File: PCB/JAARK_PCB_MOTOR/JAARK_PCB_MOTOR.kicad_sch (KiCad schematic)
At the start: 12 parts, among them IC1 TPS564242DRLR

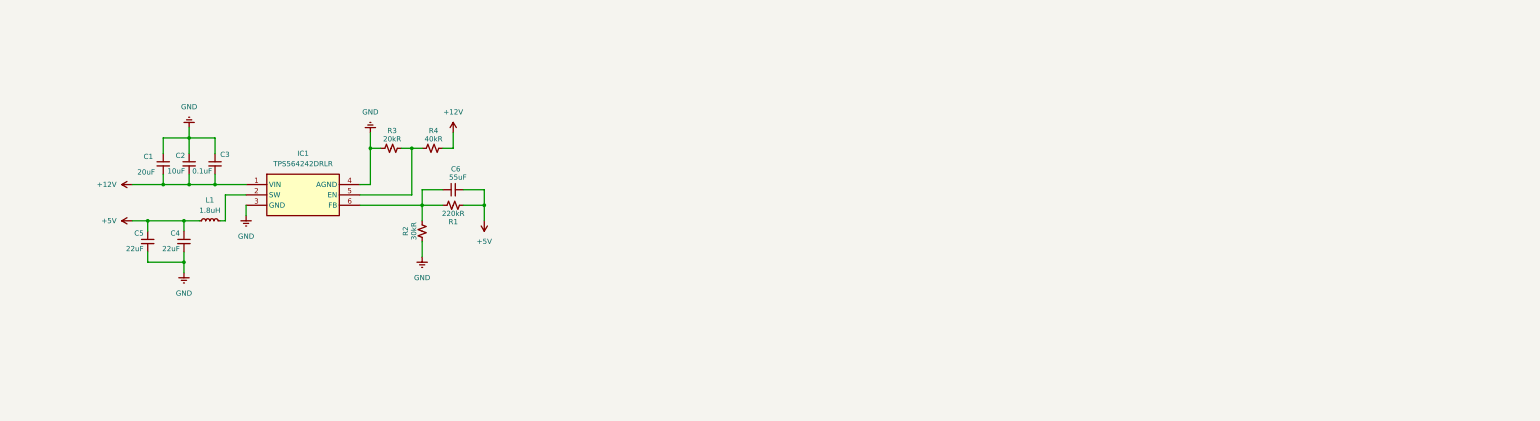
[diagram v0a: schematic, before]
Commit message: Work on Motor Driver H-Bridge. May need to consider switching to MOSFET, as BJT's are not suitable for high amp loads. Could fry board or resistors with the current H-Bridge setup.
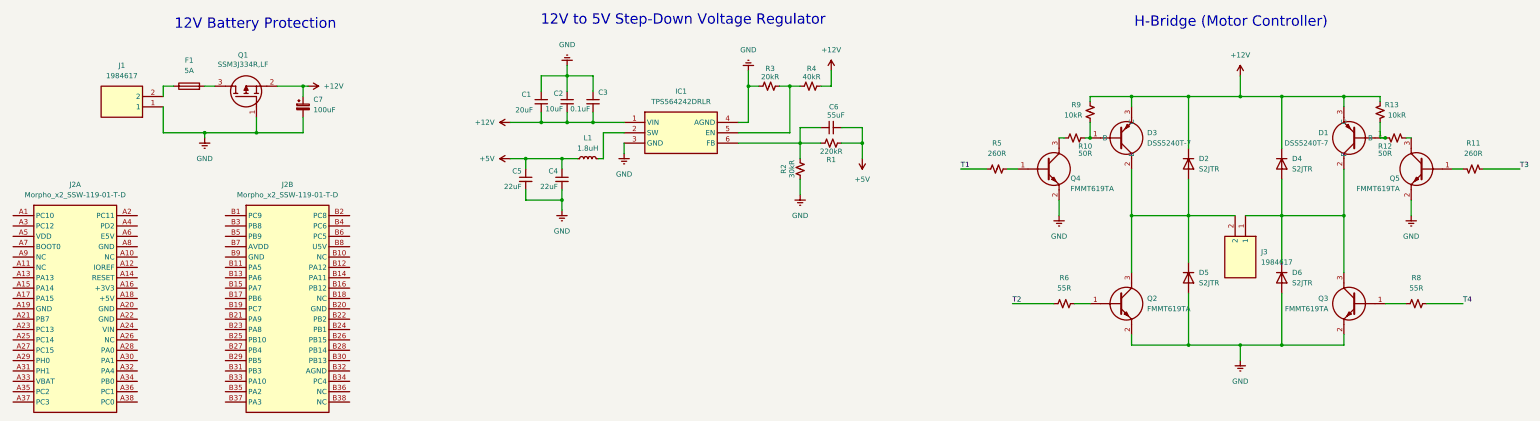
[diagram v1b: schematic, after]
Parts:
- added C7: 100uF, symbol Device:C_Polarized_Small
- added D1, D3: DSS5240T-7, SOT96P240X110-3N, symbol SSys_Parts:DSS5240T-7
- added D2, D4, D5, D6: S2JTR, Diode_SMD:D_SMB, symbol Diode:S2JTR
- added F1: 5A, symbol Device:Fuse
- added J1, J3: 1984617, 1984617, symbol SSys_Parts:1984617
- added J2: Morpho_x2_SSW-119-01-T-D, footprint_library:STM_Nucleo_Morpho_x2_Footprint, symbol sym_library:Morpho_x2_SSW-119-01-T-D
- added Q1: SSM3J334R,LF, 2SC2712GRLF, symbol SSys_Parts:SSM3J334R,LF
- added Q2, Q3, Q4, Q5: FMMT619TA, SOT95P237X112-3N, symbol SSys_Parts:FMMT619TA
- added R10, R12: 50R, symbol Device:R_Small_US
- added R11, R5: 260R, symbol Device:R_Small_US
- added R13, R9: 10kR, symbol Device:R_Small_US
- added R6, R8: 55R, symbol Device:R_Small_US
- IC1: footprint SOTFL50P160X60-6N -> SSys_Footprints:SOTFL50P160X60-6N
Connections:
- net +12V: now also C7.1, D1.3 (C), D2.1 (K), D3.3 (C), D4.1 (K), Q1.2 (S), R13.1, R9.1
- net GND: now also C7.2, D5.2 (A), D6.2 (A), J1.1, Q1.1 (G), Q2.2 (E), Q3.2 (E), Q4.2 (E), Q5.2 (E)
- new net: F1.1, J1.2
- new net: D1.1 (B), R12.2, R13.2
- new net: Q5.1 (B), R11.2
- new net: Q5.3 (C), R12.1
- new net: D1.2 (E), D4.2 (A), D6.1 (K), J3.1, Q3.3 (C)
- new net: D2.2 (A), D3.2 (E), D5.1 (K), J3.2, Q2.3 (C)
- new net: Q3.1 (B), R8.1
- new net: Q2.1 (B), R6.2
- new net: F1.2, Q1.3 (D)
- new net: D3.1 (B), R10.2, R9.2
- new net: Q4.1 (B), R5.2
- new net: Q4.3 (C), R10.1
- new net T1: R5.1
- new net T2: R6.1
- new net T3: R11.1
- new net T4: R8.2
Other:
- note added: "12V Battery Protection"
- note added: "12V to 5V Step-Down Voltage Regulator"
- note added: "H-Bridge (Motor Controller)"
- moved on the sheet: C1, C2, C3, C4, C5, C6, IC1, L1, R1, R2, R3, R4

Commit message: Finished H-Bridge
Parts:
- removed D1, D3: DSS5240T-7, SOT96P240X110-3N, symbol SSys_Parts:DSS5240T-7
- removed D2, D4, D5, D6: S2JTR, Diode_SMD:D_SMB, symbol Diode:S2JTR
- removed J3: 1984617, 1984617, symbol SSys_Parts:1984617
- removed Q2: FMMT619TA, SOT95P237X112-3N, symbol SSys_Parts:FMMT619TA
- removed R10, R12: 50R, symbol Device:R_Small_US
- removed R11, R5: 260R, symbol Device:R_Small_US
- removed R13, R9: 10kR, symbol Device:R_Small_US
- removed R6, R8: 55R, symbol Device:R_Small_US
- added D10, D11, D8, D9: S2JTR, Diode_SMD:D_SMB, symbol Diode:S2JTR
- added IC2, IC3: PJA3404_R1_00001, SOT95P240X110-3N, symbol SSys_Parts:PJA3404_R1_00001
- added J4: ${SIM.PARAMS}, 1984617, symbol SSys_Parts:1984617
- added Q2, Q6: SSM3J334RLF, 2SC2712GRLF, symbol SSys_Parts:SSM3J334R,LF
- added Q7: FMMT619TA, SOT95P237X112-3N, symbol SSys_Parts:FMMT619TA
- added R14, R16, R21, R22: 260R, symbol Device:R_Small_US
- added R15, R17, R18, R7: 5kR, symbol Device:R_Small_US
- added R19, R20: 10kR, symbol Device:R_Small_US
- added V1: 12, symbol Simulation_SPICE:VDC
- added V2: 3.3, symbol Simulation_SPICE:VDC
- added V3: 0, symbol Simulation_SPICE:VDC
- J1: value 1984617 -> ${SIM.PARAMS}
- Q1: value SSM3J334R,LF -> SSM3J334RLF; Spice_Node_Sequence (none) -> 3 1 2 2
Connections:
- net +12V: now also D10.1 (K), D8.1 (K), Q2.2 (S), Q6.2 (S), R15.1, R18.2, R19.1, R20.1
- net GND: now also D11.2 (A), D9.2 (A), IC2.2 (S), IC3.2 (S), Q7.2 (E), V1.2, V2.2, V3.2
- net T1: now also R14.2, R21.2, V3.1
- net T2: now also R16.2, R22.1, V2.1
- net at F1.1, J1.2: now also V1.1
- net at Q5.1 (B): now also R16.1
- net at Q5.3 (C): now also R17.2
- net at Q3.3 (C): now also IC3.1 (G), R20.2
- net at Q3.1 (B): now also R22.2
- net at Q4.1 (B): now also R14.1
- net at Q4.3 (C): now also R7.2
- new net: Q6.1 (G), R17.1, R18.1
- new net: D8.2 (A), D9.1 (K), IC2.3 (D), J4.2, Q2.3 (D)
- new net: IC2.1 (G), Q7.3 (C), R19.2
- new net: Q7.1 (B), R21.1
- new net: D10.2 (A), D11.1 (K), IC3.3 (D), J4.1, Q6.3 (D)
- new net: Q2.1 (G), R15.2, R7.1
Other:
- moved on the sheet: J1

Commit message: Organizing libraries in the local folder.
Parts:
- IC1: footprint SSys_Footprints:SOTFL50P160X60-6N -> JAARK_lib:SOTFL50P160X60-6N
- IC2, IC3: footprint SOT95P240X110-3N -> SSys_Footprints:SOT95P240X110-3N
- J1, J4: footprint 1984617 -> SSys_Footprints:1984617
- Q1, Q2, Q6: footprint 2SC2712GRLF -> SSys_Footprints:2SC2712GRLF
- Q3, Q4, Q5, Q7: footprint SOT95P237X112-3N -> SSys_Footprints:SOT95P237X112-3N
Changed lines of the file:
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@@
 			)
 		)
-		(property "Footprint" "1984617"
+		(property "Footprint" "SSys_Footprints:1984617"
 			(at 34.29 -51.74 0)
 			(effects
@@
 			)
 		)
-		(property "Footprint" "SOT95P240X110-3N"
+		(property "Footprint" "SSys_Footprints:SOT95P240X110-3N"
 			(at 297.18 183.82 0)
 			(effects
@@
 			)
 		)
-		(property "Footprint" "SOT95P240X110-3N"
+		(property "Footprint" "SSys_Footprints:SOT95P240X110-3N"
 			(at 339.09 183.82 0)
 			(effects
@@
 			)
 		)
-		(property "Footprint" "SOT95P237X112-3N"
+		(property "Footprint" "SSys_Footprints:SOT95P237X112-3N"
 			(at 280.67 216.84 0)
 			(effects
@@
 			)
 		)
-		(property "Footprint" "1984617"
+		(property "Footprint" "SSys_Footprints:1984617"
 			(at 225.12 83.82 0)
 			(effects
@@
 			)
 		)
-		(property "Footprint" "2SC2712GRLF"
+		(property "Footprint" "SSys_Footprints:2SC2712GRLF"
 			(at 186.36 34.29 0)
 			(effects
@@
 			)
 		)
-		(property "Footprint" "SOT95P237X112-3N"
+		(property "Footprint" "SSys_Footprints:SOT95P237X112-3N"
 			(at 355.6 216.84 0)
 			(effects
@@
 			)
 		)
-		(property "Footprint" "SOT95P237X112-3N"
+		(property "Footprint" "SSys_Footprints:SOT95P237X112-3N"
 			(at 280.67 160.96 0)
 			(effects
@@
 			)
 		)
-		(property "Footprint" "2SC2712GRLF"
+		(property "Footprint" "SSys_Footprints:2SC2712GRLF"
 			(at 340.36 -53.01 0)
 			(effects
@@
 			)
 		)
-		(property "Footprint" "SOT95P237X112-3N"
+		(property "Footprint" "SSys_Footprints:SOT95P237X112-3N"
 			(at 355.6 160.96 0)
 			(effects
@@
 			)
 		)
-		(property "Footprint" "SSys_Footprints:SOTFL50P160X60-6N"
+		(property "Footprint" "JAARK_lib:SOTFL50P160X60-6N"
 			(at 201.93 141.91 0)
 			(effects
@@
 			)
 		)
-		(property "Footprint" "2SC2712GRLF"
+		(property "Footprint" "SSys_Footprints:2SC2712GRLF"
 			(at 295.91 -53.01 0)
 			(effects

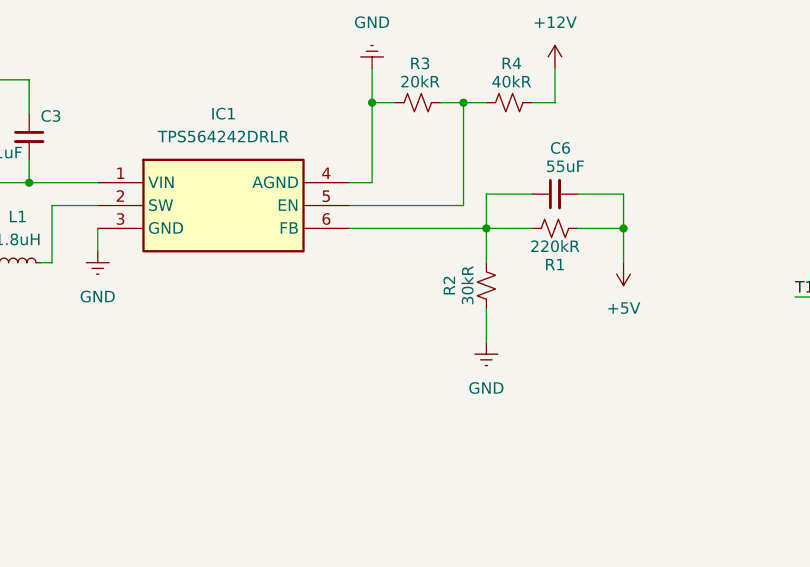
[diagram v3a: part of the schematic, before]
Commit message: Starting zephyr testing
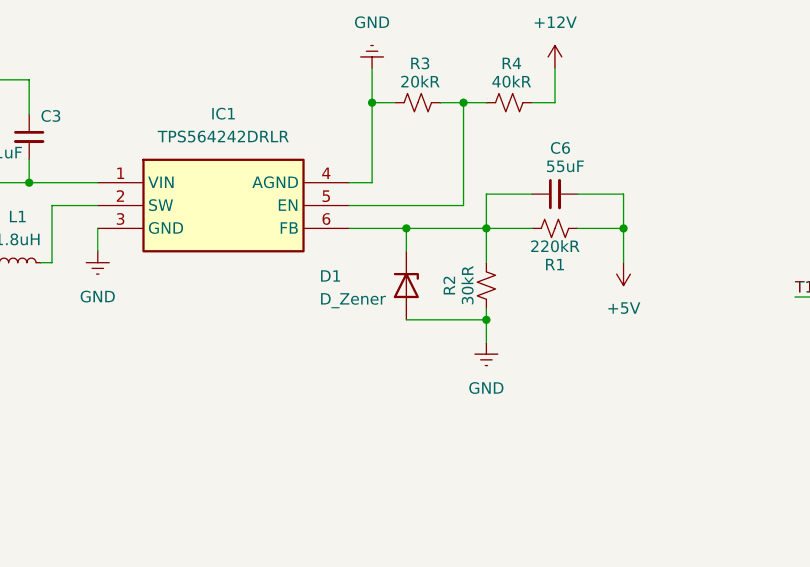
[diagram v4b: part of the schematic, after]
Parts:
- added D1: D_Zener, symbol Device:D_Zener
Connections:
- net GND: now also D1.2 (A)
- net at C6.1, IC1.6 (FB), R1.2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: now also D1.1 (K)
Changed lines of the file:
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@@
 	)
 	(junction
+		(at 220.98 62.23)
+		(diameter 0)
+		(color 0 0 0 0)
+	)
+	(junction
 		(at 236.22 52.07)
 		(diameter 0)
@@
 	)
 	(junction
+		(at 212.09 52.07)
+		(diameter 0)
+		(color 0 0 0 0)
+	)
+	(junction
 		(at 162.56 66.04)
 		(diameter 0)
@@
 	(wire
 		(pts
-			(xy 205.74 52.07) (xy 220.98 52.07)
+			(xy 205.74 52.07) (xy 212.09 52.07)
 		)
 		(stroke
@@
 	(wire
 		(pts
+			(xy 212.09 62.23) (xy 220.98 62.23)
+		)
+		(stroke
+			(width 0)
+			(type default)
+		)
+	)
+	(wire
+		(pts
+			(xy 212.09 52.07) (xy 220.98 52.07)
+		)
+		(stroke
+			(width 0)
+			(type default)
+		)
+	)
+	(wire
+		(pts
 			(xy 328.93 67.31) (xy 328.93 90.17)
 		)
@@
 	(wire
 		(pts
-			(xy 220.98 60.96) (xy 220.98 64.77)
+			(xy 220.98 60.96) (xy 220.98 62.23)
 		)
 		(stroke
@@
 	(wire
 		(pts
+			(xy 212.09 52.07) (xy 212.09 54.61)
+		)
+		(stroke
+			(width 0)
+			(type default)
+		)
+	)
+	(wire
+		(pts
 			(xy 292.1 38.1) (xy 306.07 38.1)
 		)
@@
 	(wire
 		(pts
+			(xy 220.98 62.23) (xy 220.98 64.77)
+		)
+		(stroke
+			(width 0)
+			(type default)
+		)
+	)
+	(wire
+		(pts
 			(xy 344.17 67.31) (xy 344.17 55.88)
 		)
@@
 					(unit 1)
 				)
+			)
+		)
+	)
+	(symbol
+		(lib_id "Device:D_Zener")
+		(at 212.09 58.42 270)
+		(unit 1)
+		(exclude_from_sim no)
+		(in_bom yes)
+		(on_board yes)
+		(dnp no)
+		(property "Reference" "D1"
+			(at 202.438 57.404 90)
+			(effects
+				(font
+					(size 1.27 1.27)
+				)
+				(justify left)
+			)
+		)
+		(property "Value" "D_Zener"
+			(at 202.438 59.944 90)
+			(effects
+				(font
+					(size 1.27 1.27)
+				)
+				(justify left)
+			)
+		)
+		(property "Footprint" ""
+			(at 212.09 58.42 0)
+			(effects
+				(font
+					(size 1.27 1.27)
+				)
+				(hide yes)
+			)
+		)
+		(property "Datasheet" "~"
+			(at 212.09 58.42 0)
+			(effects
+				(font
+					(size 1.27 1.27)
+				)
+				(hide yes)
+			)
+		)
+		(property "Description" "Zener diode"
+			(at 212.09 58.42 0)
+			(effects
+				(font
+					(size 1.27 1.27)
+				)
+				(hide yes)
+			)
+		)
+		(pin "1"
+		)
+		(pin "2"
+		)
+		(instances
+			(project ""
+				(path "/855a2ad7-0ca6-4188-a452-4c1fc0d76ca5"
+					(reference "D1")
+					(unit 1)
+				)

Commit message: Motor driver recreation, appended footprints to lots of R,L,C elements
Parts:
- removed IC3: PJA3404_R1_00001, SSys_Footprints:SOT95P240X110-3N, symbol SSys_Parts:PJA3404_R1_00001
- added C8: 22uF, JAARK_lib:CAPC2012X95N, symbol JAARK_lib:CL21B104KBCNNNC
- added IC3, IC5, IC6, IC7, IC8: PJA3404_R1_00001, SOT95P240X110-3N, symbol JAARK_lib:SSM3J334R,LF
- added IC4: HIP4080AIBZT, SOIC127P1032X265-20N, symbol JAARK_lib:HIP4080AIBZT
- added J3: ~, SSys_Footprints:1984617, symbol SSys_Parts:1984617
- C1: value 20uF -> 22uF; footprint (none) -> JAARK_lib:CAPC2012X95N; symbol Device:C_Small -> JAARK_lib:CL21B104KBCNNNC; Arrow Part Number (none) -> CL21B104KBCNNNC; Arrow Price/Stock (none) -> https://www.arrow.com/en/products/cl21b104kbcnnnc/samsung-e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; Height (none) -> 0.95; MPN (none) -> CL21A226MAYNNNE; Manufacturer_Name (none) -> SAMSUNG; Manufacturer_Part_Number (none) -> CL21B104KBCNNNC; Mouser Part Number (none) -> 187-CL21B104KBCNNNC; Mouser Price/Stock (none) -> https://www.mouser.co.uk/ProductDetail/Samsung-Electro-Mech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
- C2: footprint (none) -> JAARK_lib:CAPC2012X145N; Arrow Part Number (none) -> CL21A106KAYNNNG; Arrow Price/Stock (none) -> https://www.arrow.com/en/products/cl21a106kaynnng/samsung-e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; Height (none) -> 1.45; Manufacturer_Name (none) -> SAMSUNG; Manufacturer_Part_Number (none) -> CL21A106KAYNNNG; Mouser Part Number (none) -> 187-CL21A106KAYNNNG; Mouser Price/Stock (none) -> https://www.mouser.co.uk/ProductDetail/Samsung-Electro-Mech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
- C3: footprint (none) -> C0805; Arrow Part Number (none) -> C0805C104K5RACTU; Arrow Price/Stock (none) -> https://www.arrow.com/en/products/c0805c104k5ractu/kemet-co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; Height (none) -> 1.1; Manufacturer_Name (none) -> KEMET; Manufacturer_Part_Number (none) -> C0805C104K5RACTU; Mouser Part Number (none) -> 80-C0805C104K5R; Mouser Price/Stock (none) -> https://www.mouser.co.uk/ProductDetail/KEMET/C0805C104K5RAC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
- C4, C5: footprint (none) -> JAARK_lib:CAPC2012X95N; symbol Device:C_Small -> JAARK_lib:CL21B104KBCNNNC; Arrow Part Number (none) -> CL21B104KBCNNNC; Arrow Price/Stock (none) -> https://www.arrow.com/en/products/cl21b104kbcnnnc/samsung-e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; Height (none) -> 0.95; Manufacturer_Name (none) -> SAMSUNG; Manufacturer_Part_Number (none) -> CL21B104KBCNNNC; Mouser Part Number (none) -> 187-CL21B104KBCNNNC; Mouser Price/Stock (none) -> https://www.mouser.co.uk/ProductDetail/Samsung-Electro-Mech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
- C6: value 55uF -> 33uF; footprint (none) -> JAARK_lib:CAPC3216X180N; Arrow Part Number (none) -> C3216X5R1E336M160AC; Arrow Price/Stock (none) -> https://www.arrow.com/en/products/c3216x5r1e336m160ac/tdk; Height (none) -> 1.8; Manufacturer_Name (none) -> TDK; Manufacturer_Part_Number (none) -> C3216X5R1E336M160AC; Mouser Part Number (none) -> 810-C3216X5R1E336M; Mouser Price/Stock (none) -> https://www.mouser.co.uk/ProductDetail/TDK/C3216X5R1E336M16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
- IC2: footprint SSys_Footprints:SOT95P240X110-3N -> SOT95P240X110-3N; symbol SSys_Parts:PJA3404_R1_00001 -> JAARK_lib:SSM3J334R,LF
- J1: value ${SIM.PARAMS} -> dc=12
- J4: value ${SIM.PARAMS} -> ~
- L1: footprint (none) -> INDPM4141X200N; Height (none) -> 2; Manufacturer_Name (none) -> Wurth Elektronik; Manufacturer_Part_Number (none) -> 74438356018; Mouser Part Number (none) -> 710-74438356018; Mouser Price/Stock (none) -> https://www.mouser.co.uk/ProductDetail/Wurth-Elektronik/744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
- Q1, Q2, Q6: footprint SSys_Footprints:2SC2712GRLF -> 2SC2712GRLF; symbol SSys_Parts:SSM3J334R,LF -> JAARK_lib:SSM3J334R,LF
- Q3, Q4, Q5, Q7: footprint SSys_Footprints:SOT95P237X112-3N -> SOT95P237X112-3N; symbol SSys_Parts:FMMT619TA -> JAARK_lib:FMMT619TA
- R1: footprint (none) -> RESC2012X65N; Arrow Part Number (none) -> CRG0805F220K; Arrow Price/Stock (none) -> https://www.arrow.com/en/products/crg0805f220k/te-connectiv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; Height (none) -> 0.65; Manufacturer_Name (none) -> TE Connectivity; Manufacturer_Part_Number (none) -> CRG0805F220K; Mouser Part Number (none) -> 279-CRG0805F220K; Mouser Price/Stock (none) -> https://www.mouser.co.uk/ProductDetail/TE-Connectivity-Hols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
- R14, R16, R21, R22: footprint (none) -> RESC2012X60N; Height (none) -> 0.6; Manufacturer_Name (none) -> KEMET; Manufacturer_Part_Number (none) -> RC0805FR-07261RL
- R15, R17, R18, R7: footprint (none) -> RESC2012X50N; Arrow Part Number (none) -> CRCW08055K00FKTA; Arrow Price/Stock (none) -> https://www.arrow.com/en/products/crcw08055k00fkta/vishay?r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; Height (none) -> 0.5; Manufacturer_Name (none) -> Vishay; Manufacturer_Part_Number (none) -> CRCW08055K00FKTA; Mouser Part Number (none) -> 71-CRCW0805-5K; Mouser Price/Stock (none) -> https://www.mouser.co.uk/ProductDetail/Vishay-Dale/CRCW0805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
- R19, R20: footprint (none) -> RESC2012X60N; Arrow Part Number (none) -> RC0805JR-0710KL; Arrow Price/Stock (none) -> https://www.arrow.com/en/products/rc0805jr-0710kl/yageo; Height (none) -> 0.6; Manufacturer_Name (none) -> KEMET; Manufacturer_Part_Number (none) -> RC0805JR-0710KL; Mouser Part Number (none) -> 603-RC0805JR-0710KL; Mouser Price/Stock (none) -> https://www.mouser.co.uk/ProductDetail/YAGEO/RC0805JR-0710K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
- R2: footprint (none) -> RESC2012X60N; Arrow Part Number (none) -> RC0805FR-0730K1L; Arrow Price/Stock (none) -> https://www.arrow.com/en/products/rc0805fr-0730k1l/yageo?re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; Height (none) -> 0.6; Manufacturer_Name (none) -> KEMET; Manufacturer_Part_Number (none) -> RC0805FR-0730K1L; Mouser Part Number (none) -> 603-RC0805FR-0730K1L; Mouser Price/Stock (none) -> https://www.mouser.com/Search/Refine.aspx?Keyword=603-RC080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
- R3: footprint (none) -> RESC2012X50N; Height (none) -> 0.5; Manufacturer_Name (none) -> Susumu; Manufacturer_Part_Number (none) -> RG2012P-203-B-T5; Mouser Part Number (none) -> 754-RG2012P-203-B-T5; Mouser Price/Stock (none) -> https://www.mouser.co.uk/ProductDetail/Susumu/RG2012P-203-B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
- R4: footprint (none) -> JAARK_lib:RESC2012X60N; Arrow Part Number (none) -> RC0805FR-0740K2L; Arrow Price/Stock (none) -> https://www.arrow.com/en/products/rc0805fr-0740k2l/yageo; Height (none) -> 0.6; Manufacturer_Name (none) -> KEMET; Manufacturer_Part_Number (none) -> RC0805FR-0740K2L; Mouser Part Number (none) -> 603-RC0805FR-0740K2L; Mouser Price/Stock (none) -> https://www.mouser.co.uk/ProductDetail/Yageo/RC0805FR-0740K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
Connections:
- net +12V: now also C1.1; no longer C1.2
- net +5V: now also C4.2, C5.2, C8.1; no longer C4.1, C5.1
- net GND: now also C1.2, C4.1, C5.1, IC3.2 (S); no longer C1.1, C4.2, C5.2
- net at Q3.3 (C), R20.2: now also IC3.1 (G)
- net at D10.2 (A), D11.1 (K), J4.1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: now also IC3.3 (D)
- net at C6.1, D1.1 (K), IC1.6 (FB)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: now also C8.2
- new net: IC4.20 (BHO), IC5.1 (G)
- new net: IC4.19 (BHS), IC5.2 (S), IC6.3 (D), J3.2
- new net: IC5.3 (D), IC7.3 (D)
- new net: IC4.18 (BLO), IC6.1 (G)
- new net: IC6.2 (S), IC8.2 (S)
- new net: IC4.13 (ALO), IC8.1 (G)
- new net: IC4.12 (AHS), IC7.2 (S), IC8.3 (D), J3.1
- new net: IC4.11 (AHO), IC7.1 (G)
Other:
- moved on the sheet: D10, D11, D8, D9, J4, Q2, Q3, Q4, Q5, Q6, Q7, R14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

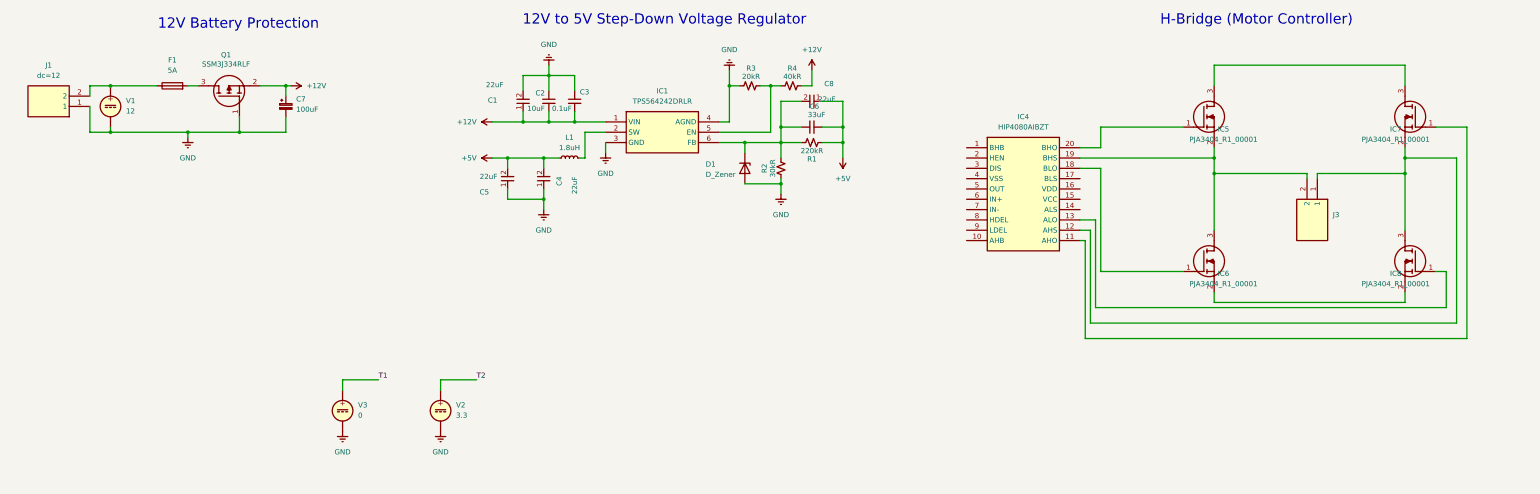
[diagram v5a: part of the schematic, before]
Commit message: Fixed footprints for sharing
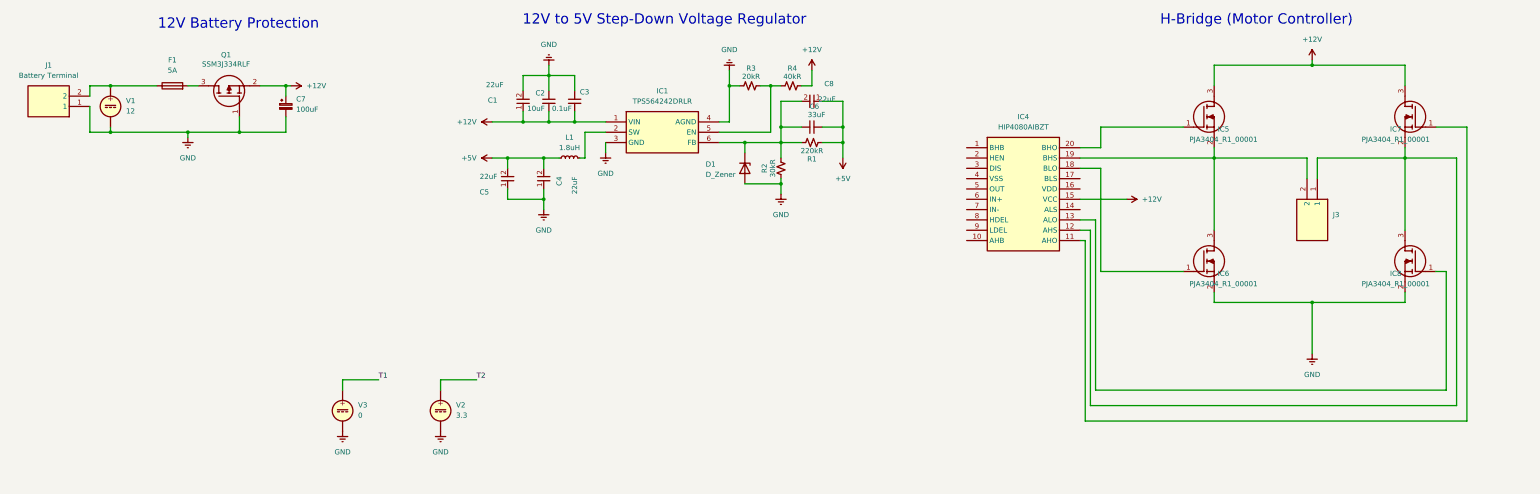
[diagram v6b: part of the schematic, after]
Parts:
- J1: value dc=12 -> Battery Terminal; footprint SSys_Footprints:1984617 -> JAARK_lib:1984617
- J3, J4: footprint SSys_Footprints:1984617 -> JAARK_lib:1984617
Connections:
- net +12V: now also IC4.15 (VCC), IC5.3 (D), IC7.3 (D)
- net GND: now also IC6.2 (S), IC8.2 (S)
